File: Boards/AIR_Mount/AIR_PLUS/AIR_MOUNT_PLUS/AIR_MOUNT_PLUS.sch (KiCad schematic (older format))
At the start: 8 parts

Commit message: First pass of High Side AIR Mount Board
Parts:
- removed D?: SS110LW, footprints:D_SOD-123W_OEM, symbol Formula:SS110LW
- removed F?: 200mA_Fuse, footprints:Fuse_1812, symbol Formula:200mA_Fuse
- removed J?: MicroFit_RA_06, footprints:MicroFit_RA_6, symbol Formula:MicroFit_RA_06
- removed J?: MicroFit_RA_08, footprints:MicroFit_RA_8, symbol Formula:MicroFit_RA_08
- removed J?: UF_4_VT, footprints:Ultrafit_4, symbol Formula:UF_4_VT
- removed K?: DBR71210(NC), footprints:D-Series_Cynergy_Relay, symbol Formula:DBR71210(NC)
- removed R?: R_3K_HS, footprints:R_3k_HS_TO247, symbol Formula:R_3K_HS
- added D1: SS110LW, footprints:D_SOD-123W_OEM, symbol formula:SS110LW
- added F1: 200mA_Fuse, footprints:Fuse_1812, symbol formula:200mA_Fuse
- added J1: UF_4_VT, footprints:Ultrafit_4, symbol footprints:UF_4_VT
- added J2: MicroFit_VT_4, footprints:MicroFit_VT_4, symbol footprints:MicroFit_VT_4
- added J3: MicroFit_RA_06, footprints:MicroFit_RA_06, symbol footprints:MicroFit_RA_06
- added J4, J5: redcude_7461166, footprints:redcube_7461166, symbol footprints:redcude_7461166
- added K1: LI12-1A85(NO), footprints:Meder-LI12, symbol formula:LI12-1A85(NO)
- added R1: R_3K_HS, footprints:R_3k_HS_TO247, symbol formula:R_3K_HS
- R2: renamed from R?; value R -> R_10K; footprint (none) -> footprints:R_TSMP_SMD_5329
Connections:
- net labels added: AIR+_AUX+, AIR+_AUX-, AIR+_COIL-, BAT+, BSPD_CURRENT_SENSOR, ENERGY_METER, FINAL_SHUTDOWN, PRECHARGE_LSD
- net labels removed: AUX+, AUX-, BSPD_Current_Sensor, CAN_Current_Sensor, Coil+, Coil-, Discharge_TS+, Discharge_TS-, E-Meter, GND, Shutdown_In, TS-
- wire segments 14 -> 12
- no-connect marks 0 -> 1
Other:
- note added: "Precharge Relay. Low Side Driven by AIR Control\n"
- note added: "TS+ Fusing"
- note added: "TSMP Body Protection Resistor"
- moved on the sheet: R2

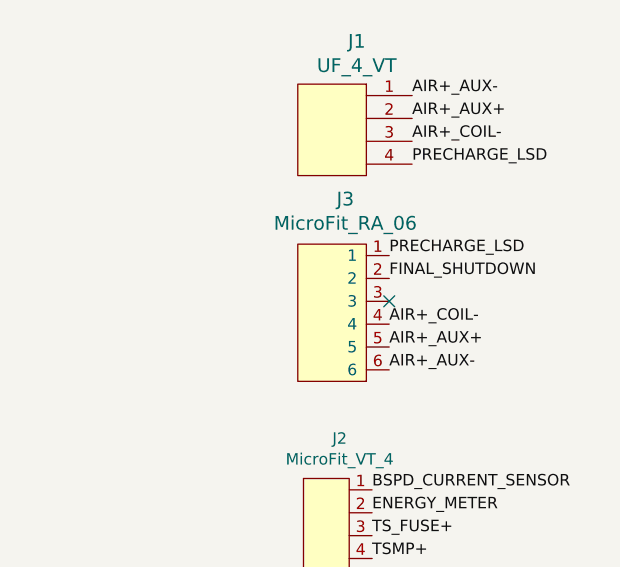
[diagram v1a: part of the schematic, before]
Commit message: new layout for air mount +
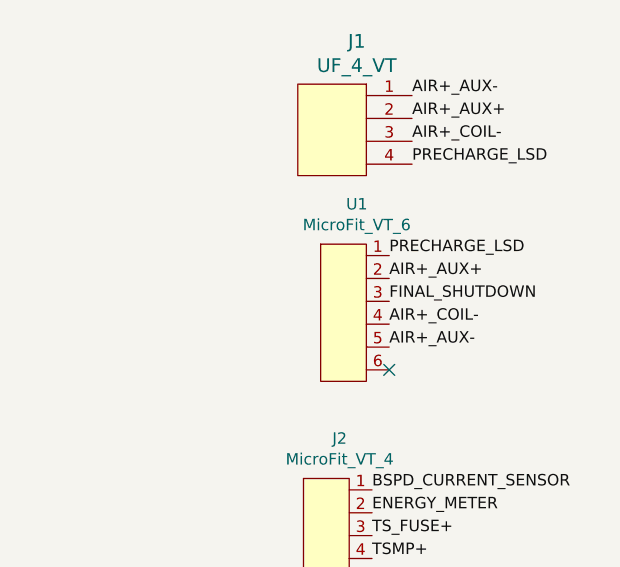
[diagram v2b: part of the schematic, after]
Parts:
- removed J3: MicroFit_RA_06, footprints:MicroFit_RA_06, symbol footprints:MicroFit_RA_06
- added U1: MicroFit_VT_6, footprints:MicroFit_VT_6, symbol footprints:MicroFit_VT_6
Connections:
- net AIR+_AUX+: now also U1.2
- net AIR+_AUX-: now also U1.5
- net AIR+_COIL-: now also U1.4
- net FINAL_SHUTDOWN: now also U1.3
- net PRECHARGE_LSD: now also U1.1
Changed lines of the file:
@@
 Text Label 4625 1800 0    50   ~ 0
 PRECHARGE_LSD
+Text Label 4625 2000 0    50   ~ 0
+FINAL_SHUTDOWN
 Text Label 4625 1900 0    50   ~ 0
-FINAL_SHUTDOWN
+AIR+_AUX+
 Text Label 4625 2200 0    50   ~ 0
-AIR+_AUX+
-Text Label 4625 2300 0    50   ~ 0
 AIR+_AUX-
 Text Label 4625 2100 0    50   ~ 0
@@
 Text Label 4725 1400 0    50   ~ 0
 PRECHARGE_LSD
-NoConn ~ 4625 2000
+NoConn ~ 4625 2300
 Wire Wire Line
 	2175 3800 2025 3800
@@
 $EndComp
 $Comp
-L footprints:MicroFit_RA_06 J3
-U 1 1 5E2586FE
-P 4375 2050
-F 0 "J3" H 4433 2547 60  0000 C CNN
-F 1 "MicroFit_RA_06" H 4433 2441 60  0000 C CNN
-F 2 "footprints:MicroFit_RA_06" H 4275 2300 60  0001 C CNN
-F 3 "https://www.molex.com/pdm_docs/sd/430450601_sd.pdf" H 4375 2400 60  0001 C CNN
-F 4 "Molex" H 4475 3450 60  0001 C CNN "MFN"
-F 5 "WM4037-ND" H 4575 3550 60  0001 C CNN "MPN"
-F 6 "https://www.digikey.com/product-detail/en/molex/0430450601/WM4037-ND/2421555" H 4375 3350 60  0001 C CNN "PurchasingLink"
-	1    4375 2050
+L footprints:MicroFit_VT_6 U1
+U 1 1 5E2CA9C7
+P 4425 2050
+F 0 "U1" H 4483 2525 50  0000 C CNN
+F 1 "MicroFit_VT_6" H 4483 2434 50  0000 C CNN
+F 2 "footprints:MicroFit_VT_6" H 4425 1650 50  0001 C CNN
+F 3 "" H 4425 2050 50  0001 C CNN
+F 4 "0430450614" H 4483 2433 50  0001 C CNN "MPN"
+F 5 "https://www.digikey.com/product-detail/en/molex/0430450614/WM1797-ND/252510" H 4483 2434 50  0001 C CNN "PurchasingLink"
+	1    4425 2050
 	1    0    0    -1
 $EndComp

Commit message: AIR mount changes
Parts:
- removed F1: 200mA_Fuse, footprints:Fuse_1812, symbol formula:200mA_Fuse
- added F1: F_1A_600V, footprints:Fuse_1A_600V, symbol Formula:F_1A_600V
- D1: symbol formula:SS110LW -> AIR_MOUNT_PLUS-rescue:SS110LW-formula
- J1: symbol footprints:UF_4_VT -> AIR_MOUNT_PLUS-rescue:UF_4_VT-footprints
- J2: symbol footprints:MicroFit_VT_4 -> AIR_MOUNT_PLUS-rescue:MicroFit_VT_4-footprints
- J4, J5: symbol footprints:redcude_7461166 -> AIR_MOUNT_PLUS-rescue:redcude_7461166-footprints
- K1: symbol formula:LI12-1A85(NO) -> AIR_MOUNT_PLUS-rescue:LI12-1A85(NO)-formula
- R1: symbol formula:R_3K_HS -> AIR_MOUNT_PLUS-rescue:R_3K_HS-formula
- U1: symbol footprints:MicroFit_VT_6 -> AIR_MOUNT_PLUS-rescue:MicroFit_VT_6-footprints
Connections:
- net BSPD_CURRENT_SENSOR: now also F1.2
- net TS+: now also F1.1
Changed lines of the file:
@@
 EESchema Schematic File Version 4
-LIBS:AIR_MOUNT_PLUS-cache
 EELAYER 30 0
 EELAYER END
@@
 TSMP+
 $Comp
-L formula:LI12-1A85(NO) K1
+L AIR_MOUNT_PLUS-rescue:LI12-1A85(NO)-formula K1
 U 1 1 5E22DF3F
 P 1850 1375
@@
 Precharge Relay. Low Side Driven by AIR Control\n
 $Comp
-L formula:R_3K_HS R1
+L AIR_MOUNT_PLUS-rescue:R_3K_HS-formula R1
 U 1 1 5E239D8B
 P 1400 1275
@@
 $EndComp
 $Comp
-L formula:SS110LW D1
+L AIR_MOUNT_PLUS-rescue:SS110LW-formula D1
 U 1 1 5E23AC7B
 P 1850 2275
@@
 $EndComp
 $Comp
-L footprints:UF_4_VT J1
+L AIR_MOUNT_PLUS-rescue:UF_4_VT-footprints J1
 U 1 1 5E23B779
 P 4375 1300
@@
 $EndComp
 $Comp
-L formula:200mA_Fuse F1
-U 1 1 5E23D965
-P 1525 3550
-F 0 "F1" H 1525 3775 50  0000 C CNN
-F 1 "200mA_Fuse" H 1525 3684 50  0000 C CNN
-F 2 "footprints:Fuse_1812" H 1475 3550 50  0001 C CNN
-F 3 "https://www.belfuse.com/resources/CircuitProtection/datasheets/0ZCG%20Nov2016.pdf" H 1475 3550 50  0001 C CNN
-F 4 "507-1767-1-ND " H 1525 3775 50  0001 C CNN "MPN"
-F 5 "https://www.digikey.com/product-detail/en/bel-fuse-inc/0ZCG0110AF2C/507-1767-1-ND/4156157" H 1525 3774 50  0001 C CNN "PurchasingLink"
-F 6 "DK" H 1525 3683 50  0001 C CNN "MFN"
-	1    1525 3550
-	1    0    0    -1
-$EndComp
-$Comp
-L footprints:redcude_7461166 J4
+L AIR_MOUNT_PLUS-rescue:redcude_7461166-footprints J4
 U 1 1 5E243056
 P 4325 3700
@@
 $EndComp
 $Comp
-L footprints:redcude_7461166 J5
+L AIR_MOUNT_PLUS-rescue:redcude_7461166-footprints J5
 U 1 1 5E244673
 P 4325 4050
@@
 TS+
 $Comp
-L footprints:MicroFit_VT_4 J2
+L AIR_MOUNT_PLUS-rescue:MicroFit_VT_4-footprints J2
 U 1 1 5E257662
 P 4350 2975
@@
 $EndComp
 $Comp
-L footprints:MicroFit_VT_6 U1
+L AIR_MOUNT_PLUS-rescue:MicroFit_VT_6-footprints U1
 U 1 1 5E2CA9C7
 P 4425 2050
@@
 	1    0    0    -1
 $EndComp
+$Comp
+L Formula:F_1A_600V F1
+U 1 1 5E5873B3
+P 1525 3550
+F 0 "F1" H 1525 3775 50  0000 C CNN
+F 1 "F_1A_600V" H 1525 3684 50  0000 C CNN
+F 2 "footprints:Fuse_1A_600V" H 1525 3250 50  0001 C CNN
+F 3 "https://media.digikey.com/pdf/Data%20Sheets/Bel%20Fuse%20PDFs/0ADAC_0ADAP_Series.pdf" H 1475 3550 50  0001 C CNN
+F 4 "https://www.digikey.com/product-detail/en/bel-fuse-inc/0ADAP1000-RE/507-2220-ND/8028479" H 1725 3900 50  0001 C CNN "PurchasingLink"
+	1    1525 3550
+	1    0    0    -1
+$EndComp

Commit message: Updating AIR Mount Boards
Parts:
- removed D1: SS110LW, footprints:D_SOD-123W_OEM, symbol AIR_MOUNT_PLUS-rescue:SS110LW-formula
- removed J1: UF_4_VT, footprints:Ultrafit_4, symbol AIR_MOUNT_PLUS-rescue:UF_4_VT-footprints
- removed J2: MicroFit_VT_4, footprints:MicroFit_VT_4, symbol AIR_MOUNT_PLUS-rescue:MicroFit_VT_4-footprints
- removed J4, J5: redcude_7461166, footprints:redcube_7461166, symbol AIR_MOUNT_PLUS-rescue:redcude_7461166-footprints
- removed K1: LI12-1A85(NO), footprints:Meder-LI12, symbol AIR_MOUNT_PLUS-rescue:LI12-1A85(NO)-formula
- removed R1: R_3K_HS, footprints:R_3k_HS_TO247, symbol AIR_MOUNT_PLUS-rescue:R_3K_HS-formula
- removed R2: R_10K, footprints:R_TSMP_SMD_5329, symbol Device:R
- removed U1: MicroFit_VT_6, footprints:MicroFit_VT_6, symbol AIR_MOUNT_PLUS-rescue:MicroFit_VT_6-footprints
- added D1: SS110LW, footprints:D_SOD-123W_OEM, symbol Formula:SS110LW
- added J1: UF_4_VT, footprints:Ultrafit_4, symbol Formula:UF_4_VT
- added J2: MicroFit_RA_06, footprints:MicroFit_RA_06, symbol Formula:MicroFit_RA_06
- added J3: MicroFit_RA_4, footprints:MicroFit_RA_4, symbol Formula:MicroFit_RA_4
- added J4, J5: redcude_7461166, footprints:redcube_7461166, symbol Formula:redcude_7461166
- added K1: DBR71210(NC), footprints:D-Series_Cynergy_Relay, symbol Formula:DBR71210(NC)
- added R1: R_3K_HS, footprints:R_3k_HS_TO247, symbol Formula:R_3K_HS
- added R2: R_10K_HV, footprints:R_TSMP_SMD_5329, symbol Formula:R_10K_HV
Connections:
- net BSPD_CURRENT_SENSOR renamed TS_Fused-
- net TS_Fused-: now also J3.2
- net TS+ renamed TS-
- net TS-: now also J3.4, J4.1, K1.1, R2.2
- new net: K1.2, R1.2
- new net AUX+: J1.1, J2.3
- new net AUX-: J1.2, J2.4
- new net BAT-: J5.1, R1.1
- new net Coil+: D1.1 (K), J1.3, J2.2, K1.4 (+)
- new net Coil-: J1.4, J2.5
- new net GND: D1.2 (A), J2.1, K1.3 (-)
- new net TSAL-: J3.1
- new net TSMP-: J3.3, R2.1
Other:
- note added: "Discharge Relay. High Side Driven by AIR Control"
- note added: "Fuse Connector"
- note added: "NEW AIR PLUS\n"
- note added: "RedCube Connectors"
- note added: "TS- Fusing"
- note added: "To AIR Control\n"
- note added: "To Relay\n"
- note removed: "Precharge Relay. Low Side Driven by AIR Control\n"
- note removed: "TS+ Fusing"
